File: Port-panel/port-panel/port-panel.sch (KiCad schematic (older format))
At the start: 4 parts

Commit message: Work on port panel
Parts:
- removed J?: RJ45, symbol Connector:RJ45
- removed J?: DB9_Female, symbol Connector:DB9_Female
- added R?: 1M, symbol Device:R
- added R? (x2): 4k7, symbol Device:R
- added TP? (x2): TestPoint, symbol Connector:TestPoint
- added U?: FT232RL, Package_SO:SSOP-28_5.3x10.2mm_P0.65mm, symbol Interface_USB:FT232RL
- added U?: MAX232, symbol Interface_UART:MAX232
- added U?: TUSB4020BIPHPR, PHP0048E_N, symbol AERO_custom_symbols:TUSB4020BIPHPR
- added U?: NCP1117-3.3_SOT223, Package_TO_SOT_SMD:SOT-223-3_TabPin2, symbol Regulator_Linear:NCP1117-3.3_SOT223
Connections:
- net VBUS: now reaches J?.1 (VBUS)
- net VBUS: now also U?.1 (VDD), U?.12 (VDD), U?.16 (VCC), U?.18 (VDD), U?.20 (VCC), U?.3 (VI), U?.30 (VDD), U?.34 (VDD), U?.4 (VCCIO), U?.45 (VDD), U?.9 (USB_VBUS)
- net USB_N: now reaches J?.2 (D-)
- net USB_N: now also U?.27 (USB_DM_UP)
- net USB_P: now reaches J?.3 (D+)
- net USB_P: now also U?.26 (USB_DP_UP)
- net GND: now reaches J?.4 (GND)
- net GND: now also J?.3, J?.6, R?.1, R?.1, R?.2, U?.1 (GND), U?.15 (GND), U?.18 (GND), U?.21 (GND), U?.25 (AGND), U?.49 (PAD), U?.7 (GND)
- net at J?.5 (Shield): now also R?.1
- net CAN_1_P: now reaches J?.1
- net CAN_1_L: now reaches J?.2
- net CAN_2_L: now reaches J?.7
- net CAN_2_P: now reaches J?.8
- new net: TP?.1, U?.2 (SCL_SMBCLK)
- new net: TP?.1, U?.3 (SDA_SMBDAT)
- new net: R?.2, U?.35 (GANGED_SMBA2_HS_UP)
- new net: R?.2, U?.36 (FULLPWRMGMT_SMBA1_N)
- new net +3V3: U?.13 (VDD33), U?.2 (VO), U?.23 (VDD33), U?.25 (VDD33), U?.33 (VDD33), U?.37 (VDD33), U?.40 (VDD33), U?.48 (VDD33), U?.7 (VDD33)
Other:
- moved on the sheet: J?

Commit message: Work on USB Hub
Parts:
- removed U?: TUSB4020BIPHPR, PHP0048E_N, symbol AERO_custom_symbols:TUSB4020BIPHPR
- removed U?: NCP1117-3.3_SOT223, Package_TO_SOT_SMD:SOT-223-3_TabPin2, symbol Regulator_Linear:NCP1117-3.3_SOT223
- added TP? (x2): TestPoint, symbol Connector:TestPoint
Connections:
- net labels added: CAN_1_N, CAN_2_N, USB_1_N, USB_1_P
- net labels removed: CAN_1_L, CAN_2_L
- wire segments 12 -> 16
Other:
- moved on the sheet: U?
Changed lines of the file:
@@
 $Descr A4 11693 8268
 encoding utf-8
-Sheet 1 1
+Sheet 1 2
 Title ""
 Date ""
@@
 CAN_1_P
 Text Label 1900 5600 0    50   ~ 0
-CAN_1_L
+CAN_1_N
 Wire Wire Line
 	1900 5600 1750 5600
@@
 USB_N
 $Comp
-L AERO_custom_symbols:TUSB4020BIPHPR U?
-U 1 1 5DAF3E9B
-P 3550 2700
-F 0 "U?" H 3550 4588 60  0000 C CNN
-F 1 "TUSB4020BIPHPR" H 3550 4482 60  0000 C CNN
-F 2 "PHP0048E_N" H 3550 2640 60  0001 C CNN
-F 3 "" H 3550 2700 60  0000 C CNN
-	1    3550 2700
-	1    0    0    -1
-$EndComp
-$Comp
 L power:VBUS #PWR?
 U 1 1 5DB0B345
@@
 	5150 1200 5450 1200
 $Comp
-L Regulator_Linear:NCP1117-3.3_SOT223 U?
-U 1 1 5DB1A1FD
-P 1250 2350
-F 0 "U?" H 1250 2592 50  0000 C CNN
-F 1 "NCP1117-3.3_SOT223" H 1250 2501 50  0000 C CNN
-F 2 "Package_TO_SOT_SMD:SOT-223-3_TabPin2" H 1250 2550 50  0001 C CNN
-F 3 "http://www.onsemi.com/pub_link/Collateral/NCP1117-D.PDF" H 1350 2100 50  0001 C CNN
-	1    1250 2350
-	1    0    0    -1
-$EndComp
-$Comp
 L power:VBUS #PWR?
 U 1 1 5DB1AD2A
@@
 $EndComp
 $Comp
-L power:GND #PWR?
-U 1 1 5DB1CC60
-P 1250 2650
-F 0 "#PWR?" H 1250 2400 50  0001 C CNN
-F 1 "GND" H 1255 2477 50  0000 C CNN
-F 2 "" H 1250 2650 50  0001 C CNN
-F 3 "" H 1250 2650 50  0001 C CNN
-	1    1250 2650
-	1    0    0    -1
-$EndComp
-$Comp
 L Connector:TestPoint TP?
 U 1 1 5DB1E232
@@
 L Interface_USB:FT232RL U?
 U 1 1 5DAE7A6D
-P 7250 2750
-F 0 "U?" H 7250 3931 50  0000 C CNN
-F 1 "FT232RL" H 7250 3840 50  0000 C CNN
-F 2 "Package_SO:SSOP-28_5.3x10.2mm_P0.65mm" H 7250 2750 50  0001 C CNN
-F 3 "http://www.ftdichip.com/Products/ICs/FT232RL.htm" H 7250 2750 50  0001 C CNN
-	1    7250 2750
+P 7300 2750
+F 0 "U?" H 7300 3931 50  0000 C CNN
+F 1 "FT232RL" H 7300 3840 50  0000 C CNN
+F 2 "Package_SO:SSOP-28_5.3x10.2mm_P0.65mm" H 7300 2750 50  0001 C CNN
+F 3 "http://www.ftdichip.com/Products/ICs/FT232RL.htm" H 7300 2750 50  0001 C CNN
+	1    7300 2750
 	1    0    0    -1
 $EndComp
@@
 $EndComp
 Wire Wire Line
-	7250 3750 7350 3750
+	7250 3750 7300 3750
 Connection ~ 7350 3750
 Wire Wire Line
-	7350 3750 7450 3750
+	7350 3750 7400 3750
 $Comp
 L power:VBUS #PWR?
@@
 $EndComp
 Text Label 1900 6100 0    50   ~ 0
-CAN_2_L
+CAN_2_N
 Text Label 1900 6200 0    50   ~ 0
 CAN_2_P
@@
 Wire Wire Line
 	1750 6200 1900 6200
+Text Label 1750 3300 0    50   ~ 0
+USB_1_P
+Text Label 1750 3400 0    50   ~ 0
+USB_1_N
+Wire Wire Line
+	1750 3300 2250 3300
+Wire Wire Line
+	1750 3400 2250 3400
+$Comp
+L Connector:TestPoint TP?
+U 1 1 5DB7353C
+P 4850 2000
+F 0 "TP?" V 4804 2188 50  0000 L CNN
+F 1 "TestPoint" V 4895 2188 50  0000 L CNN
+F 2 "" H 5050 2000 50  0001 C CNN
+F 3 "~" H 5050 2000 50  0001 C CNN
+	1    4850 2000
+	0    1    1    0
+$EndComp
+$Comp
+L Connector:TestPoint TP?
+U 1 1 5DB7498F
+P 4850 2100
+F 0 "TP?" V 4804 2288 50  0000 L CNN
+F 1 "TestPoint" V 4895 2288 50  0000 L CNN
+F 2 "" H 5050 2100 50  0001 C CNN
+F 3 "~" H 5050 2100 50  0001 C CNN
+	1    4850 2100
+	0    1    1    0
+$EndComp
+$Comp
+L power:GND #PWR?
+U 1 1 5DB75589
+P 4850 2000
+F 0 "#PWR?" H 4850 1750 50  0001 C CNN
+F 1 "GND" V 4855 1872 50  0000 R CNN
+F 2 "" H 4850 2000 50  0001 C CNN
+F 3 "" H 4850 2000 50  0001 C CNN
+	1    4850 2000
+	0    1    1    0
+$EndComp
+Text Label 6050 2350 0    50   ~ 0
+USB_1_P
+Text Label 6050 2450 0    50   ~ 0
+USB_1_N
+$Sheet
+S 3400 2350 550  300
+U 5DB772F0
+F0 "USBHUB" 50
+F1 "USBHUB.sch" 50
+F2 "USB_UP_D_P" I R 3950 2450 50
+$EndSheet
+Connection ~ 7300 3750
+Wire Wire Line
+	7300 3750 7350 3750
+Connection ~ 7400 3750
+Wire Wire Line
+	7400 3750 7450 3750
 $EndSCHEMATC

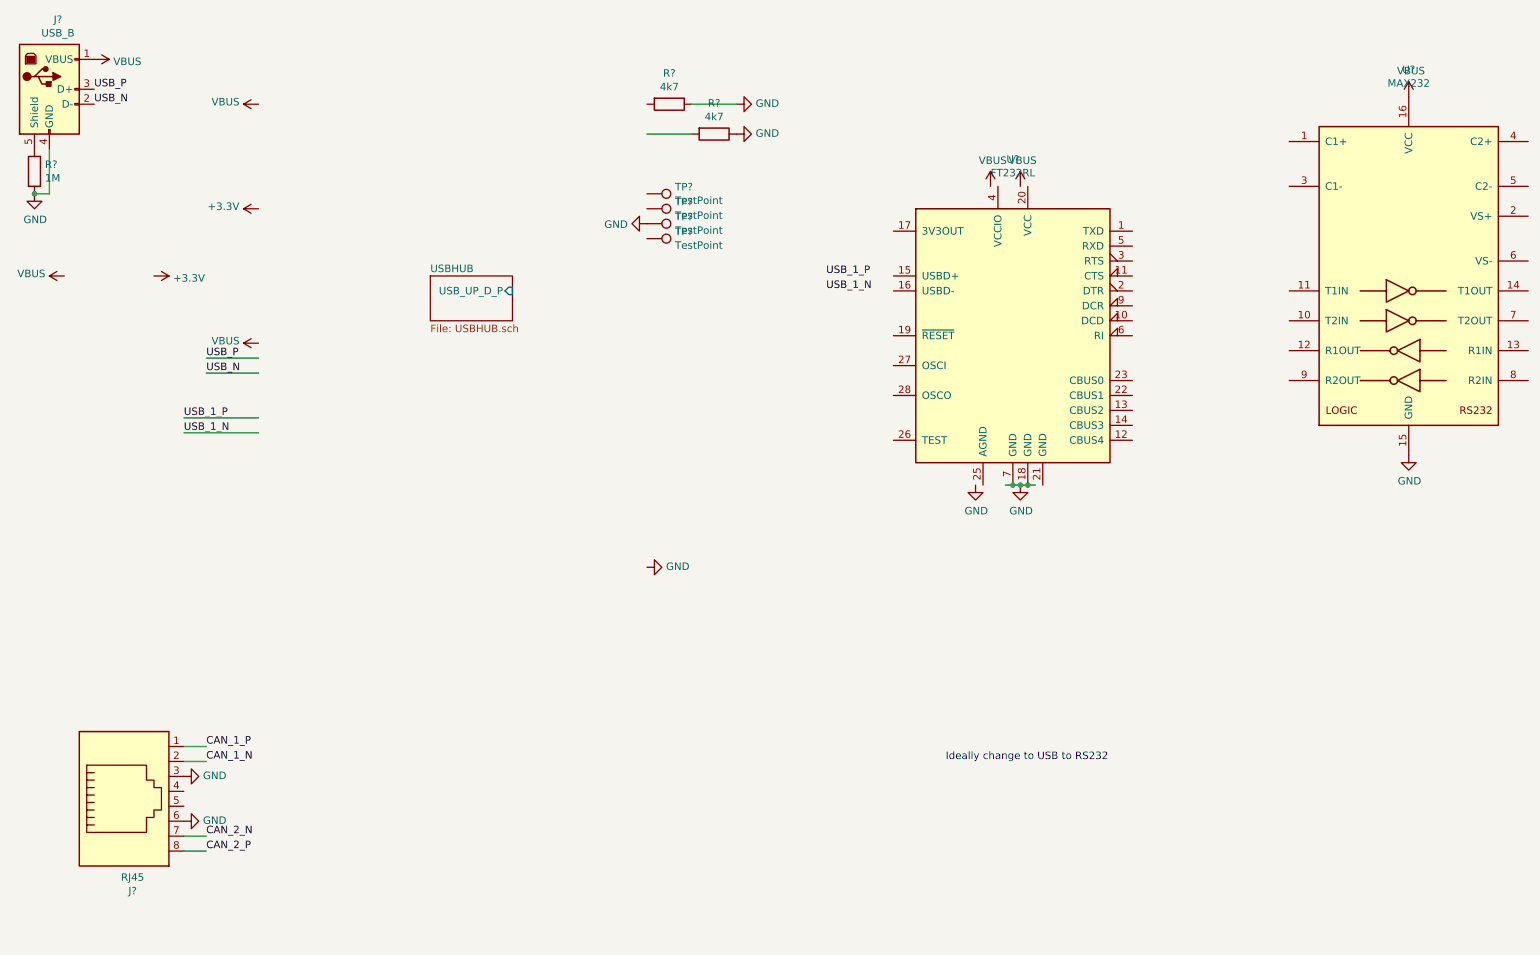
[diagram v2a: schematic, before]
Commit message: more port panel
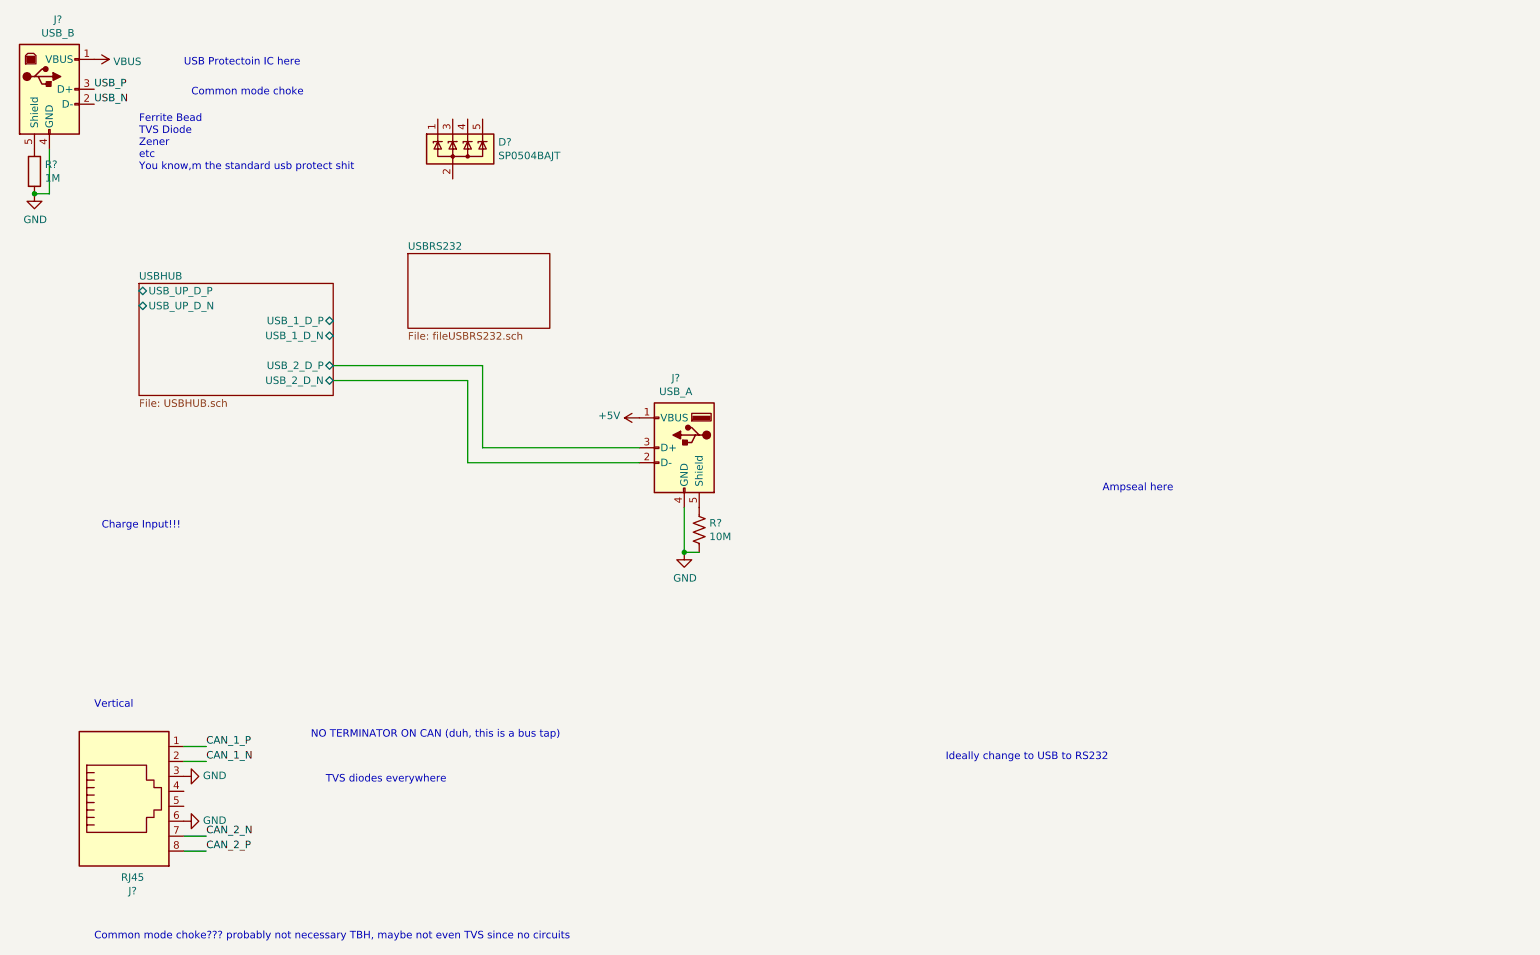
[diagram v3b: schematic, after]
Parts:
- removed R? (x2): 4k7, symbol Device:R
- removed TP? (x4): TestPoint, symbol Connector:TestPoint
- removed U?: FT232RL, Package_SO:SSOP-28_5.3x10.2mm_P0.65mm, symbol Interface_USB:FT232RL
- removed U?: MAX232, symbol Interface_UART:MAX232
- added D?: SP0504BAJT, Package_TO_SOT_SMD:SOT-353_SC-70-5, symbol Power_Protection:SP0504BAJT
- added J?: USB_A, symbol Connector:USB_A
- added R?: 10M, symbol Device:R_US
- J?: footprint (none) -> Connector_RJ:RJ45_Amphenol_RJHSE5380
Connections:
- net labels added: +5V
- net labels removed: +3.3V, USB_1_N, USB_1_P
- wire segments 16 -> 14
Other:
- note added: "Ampseal here\n"
- note added: "Charge Input!!!\n"
- note added: "Common mode choke"
- note added: "Common mode choke??? probably not necessary TBH, maybe not even TVS since no circuits"
- note added: "Ferrite Bead\nTVS Diode\nZener\netc\nYou know,m the standard usb protect shit"
- note added: "NO TERMINATOR ON CAN (duh, this is a bus tap)\n"
- note added: "TVS diodes everywhere"
- note added: "USB Protectoin IC here"
- note added: "Vertical"
